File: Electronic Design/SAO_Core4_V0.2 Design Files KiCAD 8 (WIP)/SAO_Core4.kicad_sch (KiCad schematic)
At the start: 76 parts, among them Q1 MMBT4403LT1G, Q13 MMBT4403LT1G, Q14 MMBT4401LT1G, Q17 MMBT4403LT1G, Q18 MMBT4401LT1G, Q2 MMBT4401LT1G, Q21 Q_NMOS_DGS_AO3400A, Q22 SL3401A, Q3 MMBT4403LT1G, Q4 MMBT4401LT1G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

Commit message: HWV0.2: Denote as WIP
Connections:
- net XT0,1: now also CM1.1 (XT0), CM1.2 (XT1), R21.2
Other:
- note added: "TODO: Shift LED connections up 2 pins, tying B3/4 to 7N/7P. The order will look cleaner, and LED pixel numbering will match GPB numbers."
- note removed: "Shift LED connections up 2 pins, tying B3/4 to 7N/7P. The order will look cleaner, and LED pixel numbering will match GPB numbers."
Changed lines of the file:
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@@
 		)
 	)
-	(text "Shift LED connections up 2 pins, tying B3/4  to 7N/7P. \nThe order will look cleaner, and LED pixel numbering will match GPB numbers."
-		(exclude_from_sim no)
-		(at 306.578 293.37 0)
+	(text "TODO: Shift LED connections up 2 pins, tying B3/4\nto 7N/7P. The order will look cleaner, and LED\npixel numbering will match GPB numbers."
+		(exclude_from_sim no)
+		(at 312.674 225.806 0)
 		(effects
 			(font
@@
 		)
 	)
-	(text "CORE MATRIX"
-		(exclude_from_sim no)
-		(at 306.07 82.55 0)
+	(text "CORE\nMATRIX"
+		(exclude_from_sim no)
+		(at 335.026 86.614 0)
 		(effects
 			(font
@@
 		)
 	)
+	(label "XB1"
+		(at 332.74 115.57 90)
+		(fields_autoplaced yes)
+		(effects
+			(font
+				(size 1.27 1.27)
+			)
+			(justify left bottom)
+		)
+	)
 	(label "CMDQ-1N"
 		(at 232.41 153.67 0)
@@
 		)
 	)
+	(label "XT0,1"
+		(at 332.74 83.82 90)
+		(fields_autoplaced yes)
+		(effects
+			(font
+				(size 1.27 1.27)
+			)
+			(justify left bottom)
+		)
+	)
 	(label "LED_1"
 		(at 288.29 212.09 0)
@@
 		(fields_autoplaced yes)
 		(effects
+			(font
+				(size 1.27 1.27)
+			)
+			(justify left bottom)
+		)
+	)
+	(label "XB0"
+		(at 330.2 115.57 90)
+		(fields_autoplaced yes)
+		(effects

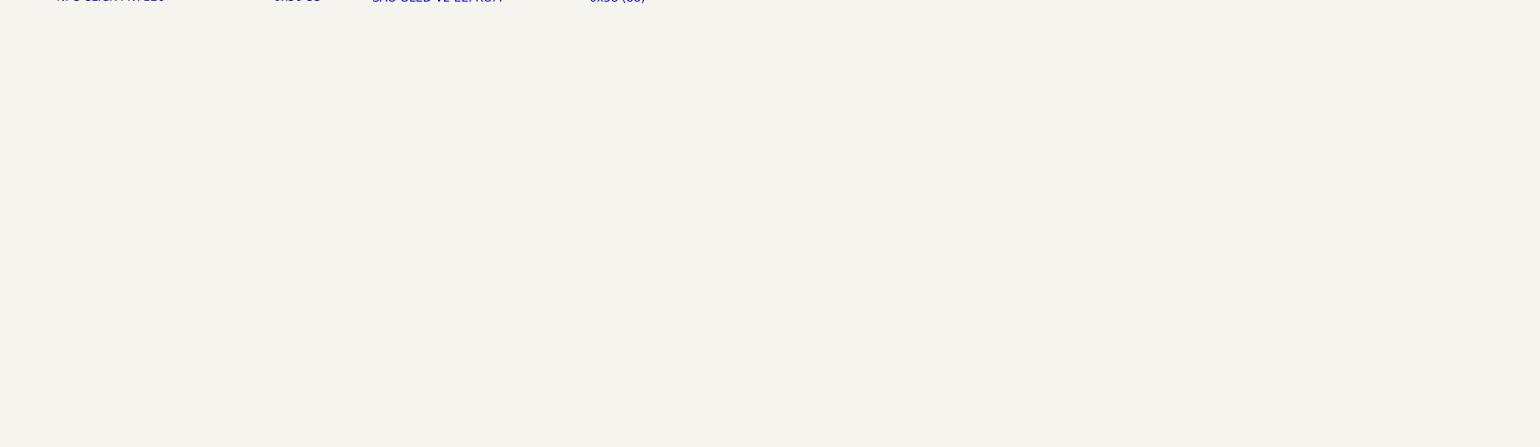
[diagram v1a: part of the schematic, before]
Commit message: Add delay after all core writes to reduce average current use
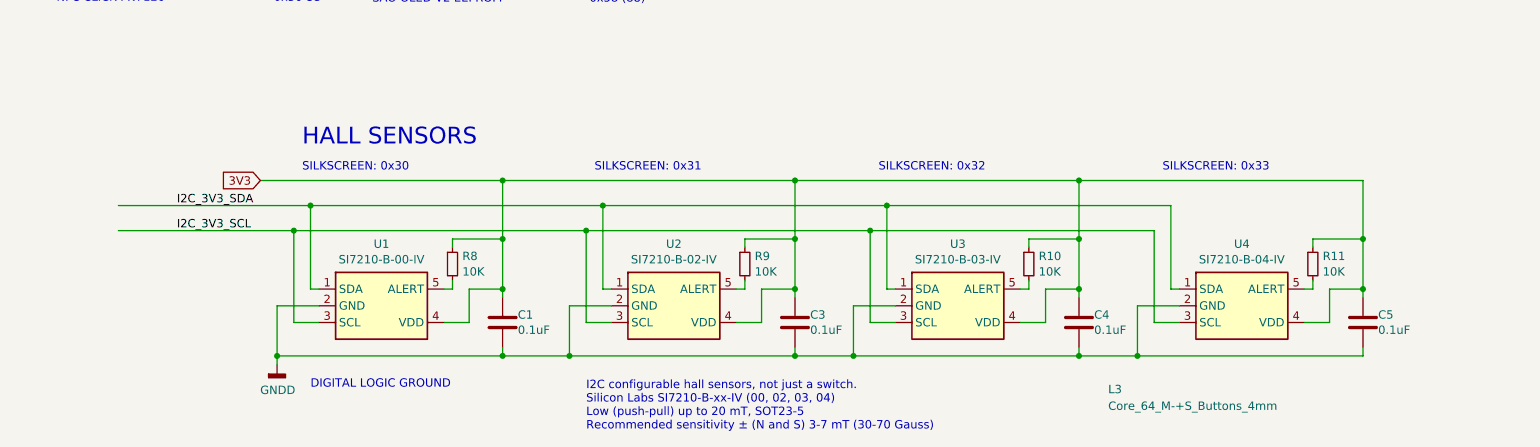
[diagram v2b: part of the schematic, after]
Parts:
- added C1, C3, C4, C5: 0.1uF, Capacitor_SMD:C_0805_2012Metric, symbol Device:C
- added L3: Core_64_M-+S_Buttons_4mm, Core_64_KiCad_Library:Core64-M_-_+_S_Buttons, symbol CORE_64_LIBRARY:Core_64_M-+S_Buttons_4mm
- added R10, R11, R8, R9: 10K, Resistor_SMD:R_0805_2012Metric, symbol Device:R_Small
- added U1: SI7210-B-00-IV, Package_TO_SOT_SMD:SOT-23-5, symbol Core64-CB-v0.6-rescue:SI7210-Sensor_Magnetic
- added U2: SI7210-B-02-IV, Package_TO_SOT_SMD:SOT-23-5, symbol Core64-CB-v0.6-rescue:SI7210-Sensor_Magnetic
- added U3: SI7210-B-03-IV, Package_TO_SOT_SMD:SOT-23-5, symbol Core64-CB-v0.6-rescue:SI7210-Sensor_Magnetic
- added U4: SI7210-B-04-IV, Package_TO_SOT_SMD:SOT-23-5, symbol Core64-CB-v0.6-rescue:SI7210-Sensor_Magnetic
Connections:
- net 3V3: now also C1.1, C3.1, C4.1, C5.1, R10.1, R11.1, R8.1, R9.1, U1.4 (VDD), U2.4 (VDD), U3.4 (VDD), U4.4 (VDD)
- new net: R10.2, U3.5 (ALERT)
- new net: R11.2, U4.5 (ALERT)
- new net: R9.2, U2.5 (ALERT)
- new net: R8.2, U1.5 (ALERT)
- new net GNDD: C1.2, C3.2, C4.2, C5.2, U1.2 (GND), U2.2 (GND), U3.2 (GND), U4.2 (GND)
- new net I2C_3V3_SCL: U1.3 (SCL), U2.3 (SCL), U3.3 (SCL), U4.3 (SCL)
- new net I2C_3V3_SDA: U1.1 (SDA), U2.1 (SDA), U3.1 (SDA), U4.1 (SDA)
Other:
- note added: "DIGITAL LOGIC GROUND"
- note added: "HALL SENSORS"
- note added: "I2C configurable hall sensors, not just a switch. Silicon Labs SI7210-B-xx-IV (00, 02, 03, 04) Low (push-pull) up to 20 mT, SOT23-5 Recommended sensitivity ± (N and S) 3-7 mT (30-70 Gauss)"
- note added: "SILKSCREEN: 0x30"
- note added: "SILKSCREEN: 0x31"
- note added: "SILKSCREEN: 0x32"
- note added: "SILKSCREEN: 0x33"
